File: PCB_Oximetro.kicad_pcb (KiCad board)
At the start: 2 copper layers, 16 parts, among them J1 USB_A, J2 Conn_01x08, U1 LM1117MP-1.8, U2 MAX30102, U3 LM1117MP-3.3, U5 ESP32-DEVKIT-V1

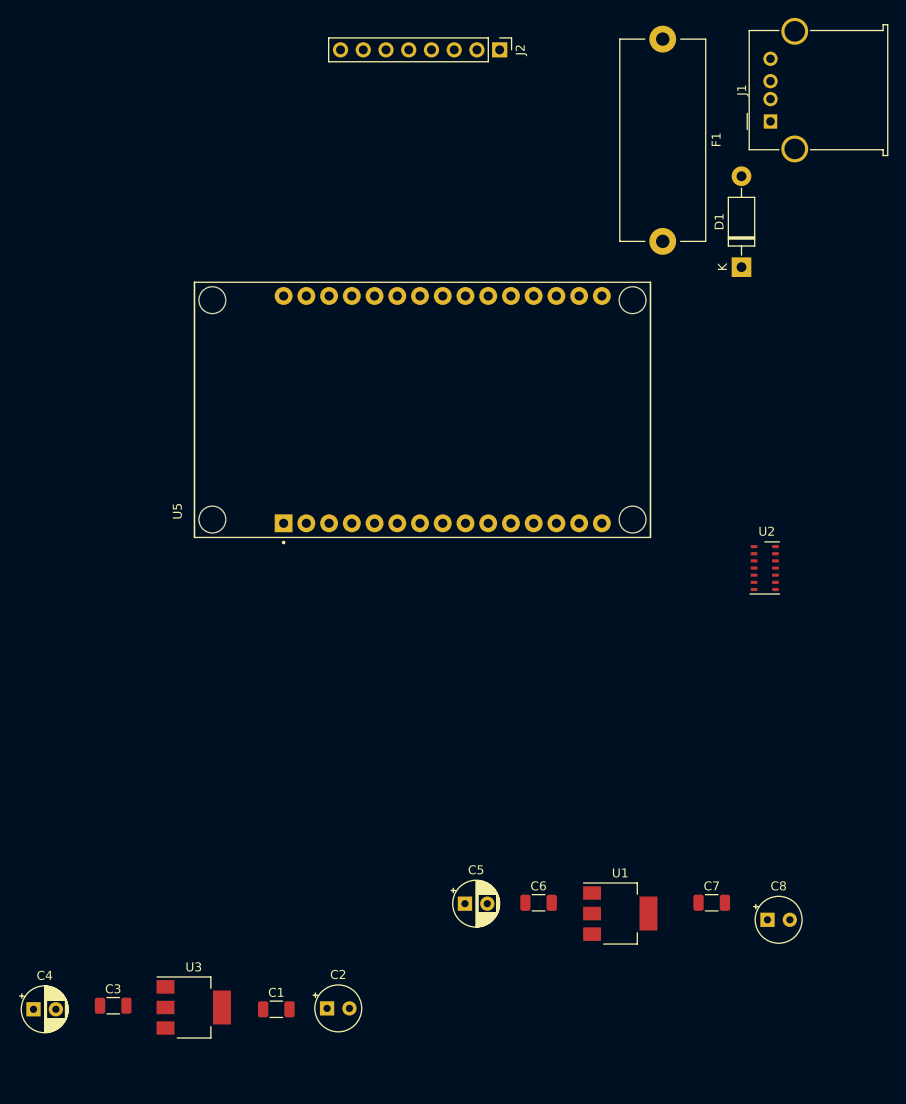
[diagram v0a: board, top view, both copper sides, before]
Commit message: PCB Layout
2nd PCB Layout (Without revision with professor)
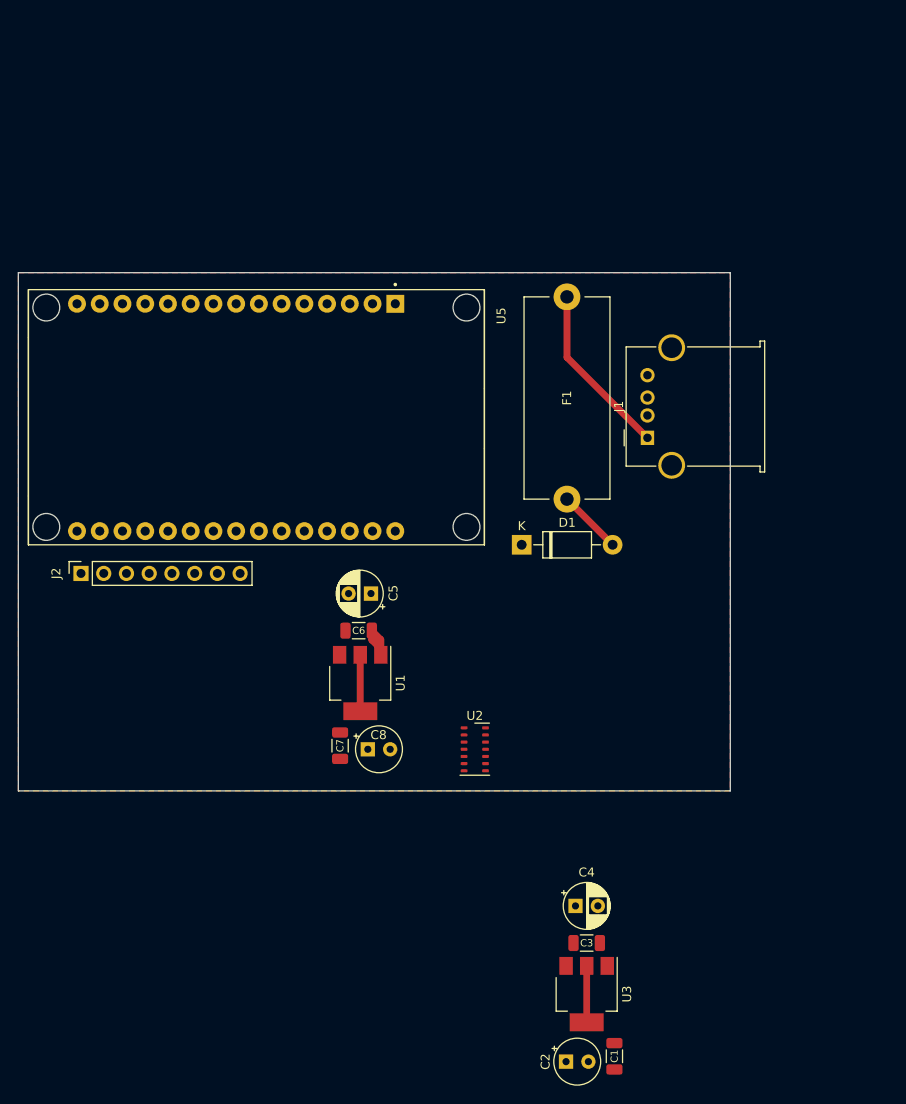
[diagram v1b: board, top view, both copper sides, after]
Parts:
- J2: footprint Connector_PinHeader_2.54mm:PinHeader_1x08_P2.54mm_Vertical -> Connector_PinSocket_2.54mm:PinSocket_1x08_P2.54mm_Vertical
- moved J2 74.9 mm to (102.9, 91.3), turned to 90 degrees
- moved C4 61.6 mm to (158.2, 128.4)
- moved C3 53.4 mm to (159.4, 132.6)
- moved C8 48.5 mm to (134.9, 111.0)
- moved C7 45.1 mm to (131.8, 110.5), turned to -90 degrees
- moved U3 43.9 mm to (159.4, 138.3), turned to -90 degrees
- moved D1 39.6 mm to (152.1, 88.1), turned to 0 degrees
- moved U1 38.8 mm to (134.1, 103.5), turned to -90 degrees
- moved U2 38.2 mm to (146.9, 111.0)
- moved C1 38.1 mm to (162.5, 145.2), turned to -90 degrees
- moved J1 37.9 mm to (166.2, 76.2)
- moved C6 36.4 mm to (133.9, 97.7)
- moved C5 36.2 mm to (135.3, 93.5), turned to 180 degrees
- moved F1 30.7 mm to (157.2, 60.4)
- moved C2 27.4 mm to (157.1, 145.8)
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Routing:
- net Net-(J1-VBUS): track 0.00 -> 19.5 mm
- net Net-(D1-A): track 0.00 -> 7.21 mm
- net 1V8: track 0.00 -> 6.30 mm
- net 3V3: track 0.00 -> 6.30 mm
- net GNDPWR: track 0.00 -> 4.95 mm
- added copper zone on F.Cu, net GNDPWR
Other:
- board outline added: 79.5 x 57.9 mm

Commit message: 3rd PCB Layout
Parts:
- moved C2 35.6 mm to (157.7, 110.3), turned to -90 degrees
- moved U3 34.7 mm to (158.9, 103.6)
- moved C1 34.7 mm to (162.0, 110.6)
- moved C3 34.7 mm to (158.9, 97.9)
- moved C4 34.7 mm to (157.7, 93.8)
- moved C5 2.57 mm to (132.7, 93.7), turned to 0 degrees
- moved C8 1.45 mm to (136.0, 110.0), turned to -90 degrees
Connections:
- U5 pad 11: SDA -> unconnected-(U5-D21-Pad11)
- U5 pad 13: INT -> unconnected-(U5-TX0-Pad13)
- U5 pad 14: SCL -> SCK
- U5 pad 26: unconnected-(U5-D14-Pad26) -> SDA
- U5 pad 27: unconnected-(U5-D12-Pad27) -> SCL
- U5 pad 28: unconnected-(U5-D13-Pad28) -> INT
- U5 pad 9: SCK -> unconnected-(U5-D18-Pad9)
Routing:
- net 3V3: track 6.30 -> 90.1 mm
- net +5V: track 0.00 -> 53.5 mm
- net INT: track 0.00 -> 32.5 mm
- net 1V8: track 6.30 -> 30.6 mm
- net GNDPWR: track 4.95 -> 9.57 mm
- net SDA: track 0.00 -> 1.24 mm
- net SCL: track 0.00 -> 0.93 mm

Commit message: 4th PCB Layout
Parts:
- added C9: 10uF, Capacitor_THT:CP_Radial_D5.0mm_P2.50mm, F.Cu at (135.9, 67.0)
- added R1: 2K2, Resistor_SMD:R_1206_3216Metric, F.Cu at (137.3, 71.8)
- added R2: 1K, Resistor_SMD:R_1206_3216Metric, B.Cu at (165.6, 92.0)
- added SW1: SW_Push, Button_Switch_THT:SW_Tactile_SPST_Angled_PTS645Vx58-2LFS, F.Cu at (172.9, 88.5)
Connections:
- U5 pad 10: MISO -> unconnected-(U5-D19-Pad10)
- U5 pad 14: SCK -> unconnected-(U5-D22-Pad14)
- U5 pad 15: MISO -> BLK
- U5 pad 19: unconnected-(U5-D34-Pad19) -> MISO
- U5 pad 21: unconnected-(U5-D32-Pad21) -> SCK
- U5 pad 22: unconnected-(U5-D33-Pad22) -> MISO
- U5 pad 23: unconnected-(U5-D25-Pad23) -> RESET
- U5 pad 24: unconnected-(U5-D26-Pad24) -> DC
- U5 pad 25: unconnected-(U5-D27-Pad25) -> CS
- U5 pad 3: unconnected-(U5-D15-Pad3) -> BTT
- U5 pad 4: BLK -> unconnected-(U5-D2-Pad4)
- U5 pad 5: CS -> unconnected-(U5-D4-Pad5)
- U5 pad 6: DC -> unconnected-(U5-RX2-Pad6)
- U5 pad 7: RESET -> unconnected-(U5-TX2-Pad7)
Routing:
- net BLK: track 0.00 -> 59.0 mm
- net BTT: track 0.00 -> 57.7 mm
- net SDA: track 1.24 -> 33.7 mm
- net SCL: track 0.93 -> 32.4 mm
- net MISO: track 0.00 -> 14.7 mm
- net +5V: track 53.5 -> 63.2 mm
- net GNDPWR: track 9.57 -> 0.30 mm
- net DC: track 0.00 -> 9.13 mm
- net RESET: track 0.00 -> 9.13 mm
- net SCK: track 0.00 -> 9.13 mm
- net CS: track 0.00 -> 9.13 mm
- net Net-(R2-Pad2): track 0.00 -> 8.10 mm
